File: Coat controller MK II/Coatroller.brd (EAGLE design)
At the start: 58.4 x 21.6 mm, 8 parts, among them U1 ATMEGA328P_PDIP, U2 V_REG_LDOSMD, Y1 ABM3B-16.000MHZ-B2-T

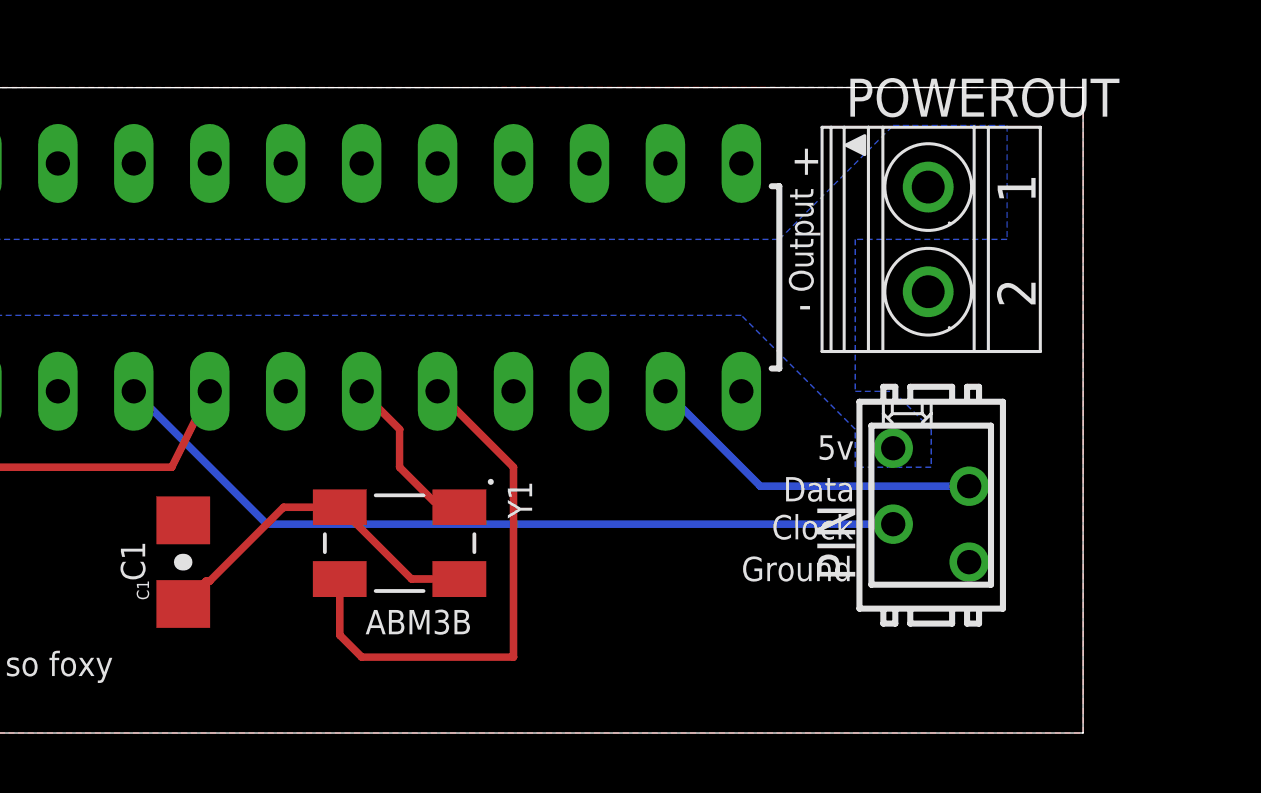
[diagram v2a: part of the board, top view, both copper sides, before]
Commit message: Fixed crystal and caps
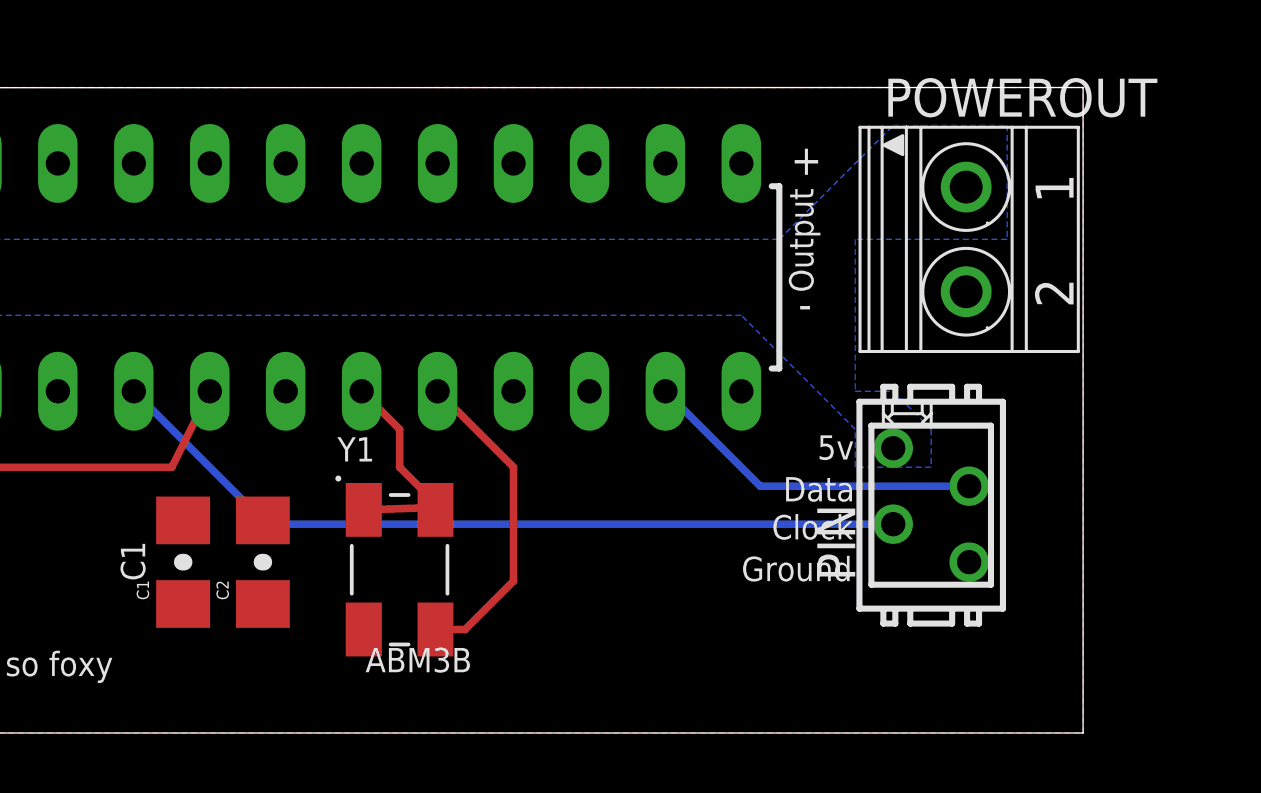
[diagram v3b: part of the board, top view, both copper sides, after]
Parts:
- added C2: (no value), SparkFun-Capacitors:1206-CAP
- moved POWEROUT 1.27 mm to (54.6, 16.5)
- moved Y1 0.89 mm to (35.6, 5.46), turned to 0 degrees
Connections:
- removed net N$3: C1.1, Y1.2, Y1.4
- net GROUND: now also C2.2, Y1.2, Y1.4
- net N$1: now also C1.1
- net N$2: now also C2.1
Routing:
- net N$3: track 11.6 -> 0.00 mm
- net N$2: track 17.9 -> 10.7 mm
- net N$1: track 5.72 -> 7.60 mm
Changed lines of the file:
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@@
 <?xml version="1.0" encoding="utf-8"?>
 <!DOCTYPE eagle SYSTEM "eagle.dtd">
-<eagle version="7.6.0">
+<eagle version="7.5.0">
 <drawing>
 <settings>
@@
 <layer number="20" name="Dimension" color="15" fill="1" visible="yes" active="yes"/>
 <layer number="21" name="tPlace" color="16" fill="1" visible="yes" active="yes"/>
-<layer number="22" name="bPlace" color="14" fill="1" visible="yes" active="yes"/>
+<layer number="22" name="bPlace" color="14" fill="1" visible="no" active="yes"/>
 <layer number="23" name="tOrigins" color="15" fill="1" visible="yes" active="yes"/>
 <layer number="24" name="bOrigins" color="15" fill="1" visible="yes" active="yes"/>
@@
 <text x="48.006" y="6.477" size="0.8128" layer="21" ratio="15">Clock</text>
 <text x="46.99" y="5.08" size="0.8128" layer="21" ratio="15">Ground</text>
-<text x="34.417" y="3.302" size="0.8128" layer="21" ratio="15">ABM3B</text>
+<text x="34.417" y="2.032" size="0.8128" layer="21" ratio="15">ABM3B</text>
 <text x="27.051" y="5.08" size="0.8128" layer="21" ratio="15" rot="R90">C1</text>
 <text x="8.89" y="14.351" size="0.8128" layer="21" ratio="15" rot="R90">Input</text>
@@
 <element name="U1" library="SparkFun-DigitalIC" package="DIL28-3" value="ATMEGA328P_PDIP" x="30.48" y="15.24"/>
 <element name="U2" library="SparkFun-PowerIC" package="SOT23-5" value="V_REG_LDOSMD" x="8.89" y="10.16" rot="R270"/>
-<element name="Y1" library="ABM3B-16.000MHZ-B2-T" package="OSCSC500X320X110-4N" value="ABM3B-16.000MHZ-B2-T" x="35.56" y="6.35" rot="R270">
-<attribute name="PRICE" value="0.52 USD" x="35.56" y="6.35" size="1.778" layer="27" rot="R270" display="off"/>
-<attribute name="MP" value="ABM3B-16.000MHZ-B2-T" x="35.56" y="6.35" size="1.778" layer="27" rot="R270" display="off"/>
-<attribute name="PACKAGE" value="5.0 x 3.2mm Abracon" x="35.56" y="6.35" size="1.778" layer="27" rot="R270" display="off"/>
-<attribute name="DESCRIPTION" value="Crystal 16MHz %3F%3F20ppm %28Tol%29 %3F%3F50ppm %28Stability%29 18pF FUND 50Ohm 4-Pin CSMD T/R" x="35.56" y="6.35" size="1.778" layer="27" rot="R270" display="off"/>
-<attribute name="MF" value="Abracon" x="35.56" y="6.35" size="1.778" layer="27" rot="R270" display="off"/>
-<attribute name="AVAILABILITY" value="Good" x="35.56" y="6.35" size="1.778" layer="27" rot="R270" display="off"/>
+<element name="Y1" library="ABM3B-16.000MHZ-B2-T" package="OSCSC500X320X110-4N" value="ABM3B-16.000MHZ-B2-T" x="35.56" y="5.461">
+<attribute name="PRICE" value="0.52 USD" x="35.56" y="5.461" size="1.778" layer="27" display="off"/>
+<attribute name="MP" value="ABM3B-16.000MHZ-B2-T" x="35.56" y="5.461" size="1.778" layer="27" display="off"/>
+<attribute name="PACKAGE" value="5.0 x 3.2mm Abracon" x="35.56" y="5.461" size="1.778" layer="27" display="off"/>
+<attribute name="DESCRIPTION" value="Crystal 16MHz %3F%3F20ppm %28Tol%29 %3F%3F50ppm %28Stability%29 18pF FUND 50Ohm 4-Pin CSMD T/R" x="35.56" y="5.461" size="1.778" layer="27" display="off"/>
+<attribute name="MF" value="Abracon" x="35.56" y="5.461" size="1.778" layer="27" display="off"/>
+<attribute name="AVAILABILITY" value="Good" x="35.56" y="5.461" size="1.778" layer="27" display="off"/>
 </element>
 <element name="POWERINPUT" library="con-phoenix-350" package="1751248" value="1751248" x="3.81" y="16.51" rot="R90">
@@
 </element>
 <element name="U$1" library="GeekAmmo" package="USB-MICRO-MOLEX-105017-0001" value="USB-CON-5PIN-105017-0001" x="0.762" y="5.334" rot="R90"/>
-<element name="POWEROUT" library="con-phoenix-350" package="1751248" value="1751248" x="53.34" y="16.51" rot="R270">
-<attribute name="MF" value="" x="53.34" y="16.51" size="1.778" layer="27" font="vector" ratio="15" rot="R270" display="off"/>
-<attribute name="OC_NEWARK" value="unknown" x="53.34" y="16.51" size="1.778" layer="27" font="vector" ratio="15" rot="R270" display="off"/>
-<attribute name="OC_FARNELL" value="unknown" x="53.34" y="16.51" size="1.778" layer="27" font="vector" ratio="15" rot="R270" display="off"/>
-<attribute name="MPN" value="" x="53.34" y="16.51" size="1.778" layer="27" font="vector" ratio="15" rot="R270" display="off"/>
+<element name="POWEROUT" library="con-phoenix-350" package="1751248" value="1751248" x="54.61" y="16.51" rot="R270">
+<attribute name="MF" value="" x="54.61" y="16.51" size="1.778" layer="27" font="vector" ratio="15" rot="R270" display="off"/>
+<attribute name="OC_NEWARK" value="unknown" x="54.61" y="16.51" size="1.778" layer="27" font="vector" ratio="15" rot="R270" display="off"/>
+<attribute name="OC_FARNELL" value="unknown" x="54.61" y="16.51" size="1.778" layer="27" font="vector" ratio="15" rot="R270" display="off"/>
+<attribute name="MPN" value="" x="54.61" y="16.51" size="1.778" layer="27" font="vector" ratio="15" rot="R270" display="off"/>
 </element>
 <element name="C1" library="SparkFun-Capacitors" package="1206-CAP" value="" x="28.321" y="5.715" rot="R90"/>
@@
 <attribute name="MPN" value="7-215464-4" x="53.34" y="7.62" size="1.778" layer="27" font="vector" ratio="15" rot="R90" display="off"/>
 </element>
+<element name="C2" library="SparkFun-Capacitors" package="1206-CAP" value="" x="30.988" y="5.715" rot="R90"/>
 </elements>
 <signals>
@@
 <contactref element="U$1" pad="5"/>
 <contactref element="U1" pad="8"/>
-<contactref element="C1" pad="2"/>
 <contactref element="PIN" pad="4"/>
 <wire x1="1.27" y1="11.43" x2="2.54" y2="12.7" width="0.254" layer="1"/>
@@
 <vertex x="58.42" y="21.59"/>
 </polygon>
+<contactref element="C1" pad="2"/>
+<contactref element="C2" pad="2"/>
+<contactref element="Y1" pad="2"/>
+<contactref element="Y1" pad="4"/>
+<wire x1="34.36" y1="3.461" x2="36.76" y2="7.461" width="0" layer="19" extent="1-1"/>
+<wire x1="30.988" y1="7.115" x2="34.36" y2="3.461" width="0" layer="19" extent="1-1"/>
 </signal>
 <signal name="VCC">
@@
 <contactref element="U1" pad="9"/>
 <wire x1="34.36" y1="11.36" x2="34.29" y2="11.43" width="0.254" layer="1"/>
-<wire x1="37.56" y1="7.55" x2="36.9" y2="7.55" width="0.254" layer="1"/>
+<wire x1="34.36" y1="7.461" x2="36.9" y2="7.55" width="0.254" layer="1"/>
 <wire x1="36.9" y1="7.55" x2="35.56" y2="8.89" width="0.254" layer="1"/>
 <wire x1="35.56" y1="8.89" x2="35.56" y2="10.16" width="0.254" layer="1"/>
 <wire x1="35.56" y1="10.16" x2="34.29" y2="11.43" width="0.254" layer="1"/>
+<contactref element="C1" pad="1"/>
+<wire x1="28.321" y1="4.315" x2="34.36" y2="7.461" width="0" layer="19" extent="1-1"/>
 </signal>
 <signal name="N$2">
 <contactref element="Y1" pad="3"/>
 <contactref element="U1" pad="10"/>
-<wire x1="33.56" y1="5.15" x2="33.56" y2="3.27" width="0.254" layer="1"/>
-<wire x1="33.56" y1="3.27" x2="34.29" y2="2.54" width="0.254" layer="1"/>
-<wire x1="34.29" y1="2.54" x2="39.37" y2="2.54" width="0.254" layer="1"/>
-<wire x1="39.37" y1="2.54" x2="39.37" y2="8.89" width="0.254" layer="1"/>
+<wire x1="36.76" y1="3.461" x2="37.751" y2="3.461" width="0.254" layer="1"/>
+<wire x1="37.751" y1="3.461" x2="39.37" y2="5.08" width="0.254" layer="1"/>
+<wire x1="39.37" y1="5.08" x2="39.37" y2="8.89" width="0.254" layer="1"/>
 <wire x1="39.37" y1="8.89" x2="36.83" y2="11.43" width="0.254" layer="1"/>
-</signal>
-<signal name="N$3">
-<contactref element="Y1" pad="4"/>
-<contactref element="Y1" pad="2"/>
-<contactref element="C1" pad="1"/>
-<wire x1="37.56" y1="5.15" x2="35.96" y2="5.15" width="0.254" layer="1"/>
-<wire x1="35.96" y1="5.15" x2="33.56" y2="7.55" width="0.254" layer="1"/>
-<wire x1="33.56" y1="7.55" x2="31.68" y2="7.55" width="0.254" layer="1"/>
-<wire x1="31.68" y1="7.55" x2="29.21" y2="5.08" width="0.254" layer="1"/>
-<wire x1="29.21" y1="5.08" x2="29.086" y2="5.08" width="0.254" layer="1"/>
-<wire x1="29.086" y1="5.08" x2="28.321" y2="4.315" width="0.254" layer="1"/>
+<contactref element="C2" pad="1"/>
+<wire x1="30.988" y1="4.315" x2="36.76" y2="3.461" width="0" layer="19" extent="1-1"/>
 </signal>
 <signal name="DATA">

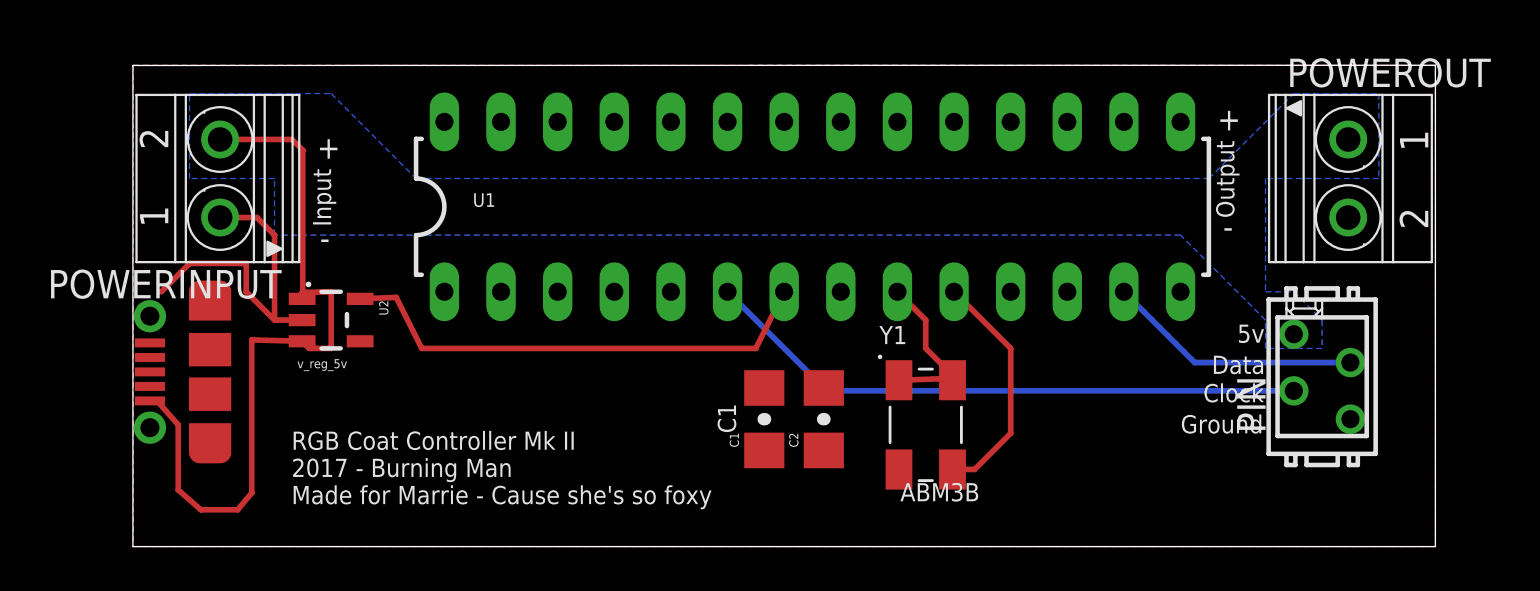
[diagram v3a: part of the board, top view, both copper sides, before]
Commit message: Fixed usb direction and fixed some routing
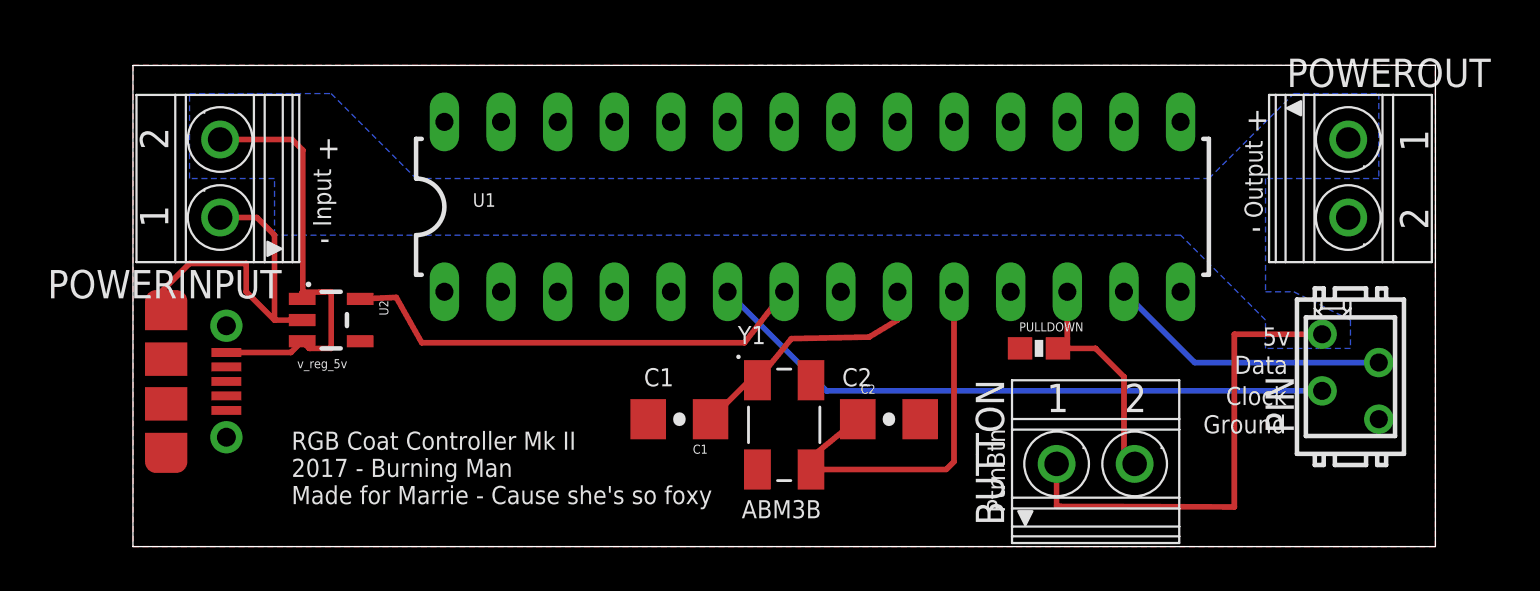
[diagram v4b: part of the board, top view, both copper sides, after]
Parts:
- added BUTTON: 1751248, con-phoenix-350:1751248
- added PULLDOWN: 10K, SparkFun-Resistors:0603-RES
- moved Y1 6.35 mm to (29.2, 5.46)
- moved U$1 5.71 mm to (4.19, 9.91), turned to 270 degrees
- moved C1 3.81 mm to (24.5, 5.71), turned to 180 degrees
- moved C2 2.92 mm to (33.9, 5.71), turned to 0 degrees
- moved PIN 1.27 mm to (54.6, 7.62)
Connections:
- new net BUTTONPIN: BUTTON.2, PULLDOWN.2, U1.12
- net GROUND: now also PULLDOWN.1
- net VCC: now also BUTTON.1
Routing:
- net BUTTONPIN: track 0.00 -> 10.3 mm
- net VCC: track 34.0 -> 41.4 mm
- net N$2: track 10.7 -> 17.4 mm
- net N$1: track 7.60 -> 11.6 mm
- net DATA: track 11.5 -> 12.7 mm
- net CLOCK: track 27.2 -> 28.5 mm
- net 5V: track 22.0 -> 21.3 mm
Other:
- board text added: "C2"
- board text added: "PtrnBtn"
